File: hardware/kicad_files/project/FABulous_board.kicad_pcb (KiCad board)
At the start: 4 copper layers, 101.2 x 63.5 mm, 79 parts, among them J1 Conn_01x03_Pin, J10 Conn_01x03_Pin, J11 Conn_01x03_Pin, J12 Conn_01x05_Pin, J2 Conn_01x03_Pin, J3 Conn_01x03_Pin, J4 Conn_01x03_Pin, J5 Conn_01x02_Socket, J6 Conn_02x04_Odd_Even, J7 Conn_02x12_Odd_Even, J8 Conn_01x03_Pin, J9 Conn_01x03_Pin, SW1 Tactile Switch, T1 LOGO, U1 W25Q32FVSS, U10 SN74LVC1G125DCKR, U11 SI5351A-B-GTR, U4 GT-USB-7010ASV, U5 FT232H, U6 AMS1117-3_3, U7 SPX1117M3-L-1-5_TR, U8 MCP1319MT-29LE-OT, U9 SN74LVC1G125DCKR, X1 TXM12M0004252DBCEO00T, X2 NX3225GA-25_000M-STD-CRG-2

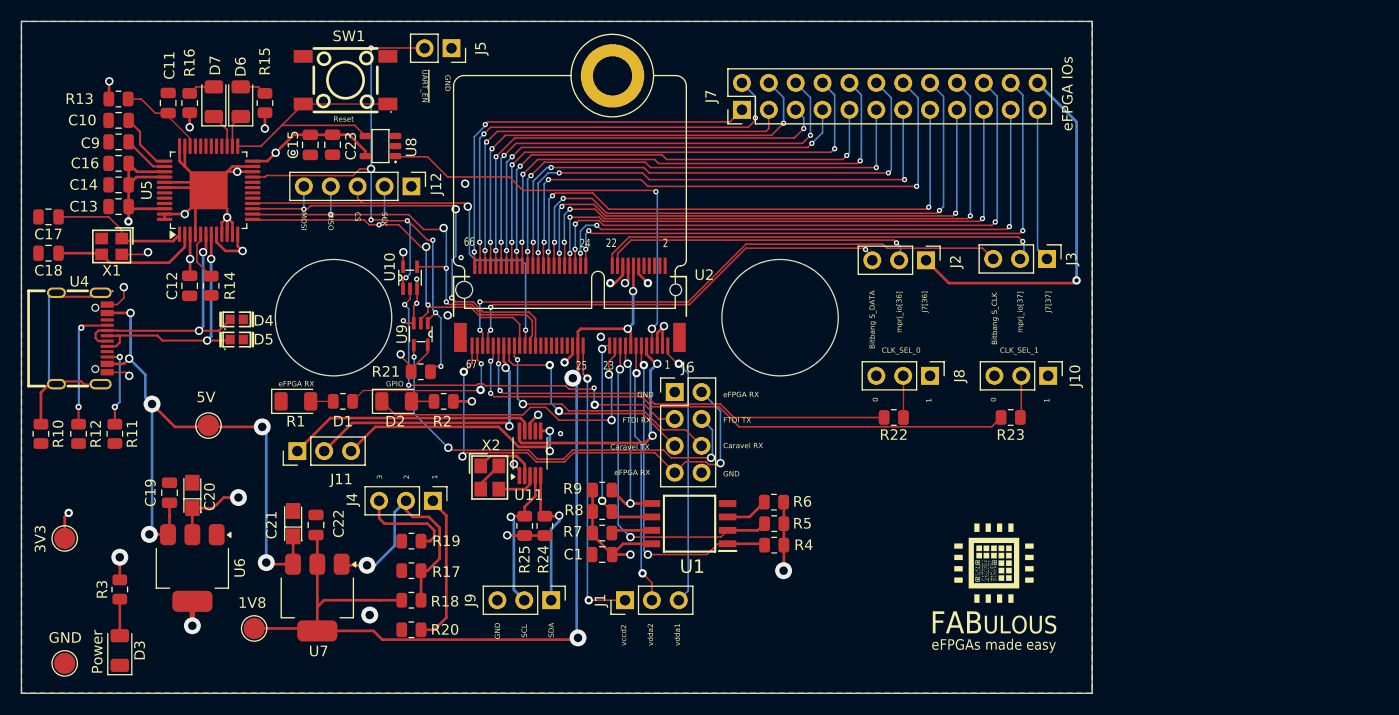
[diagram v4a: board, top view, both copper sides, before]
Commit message: feat: Implement all findings of the second review
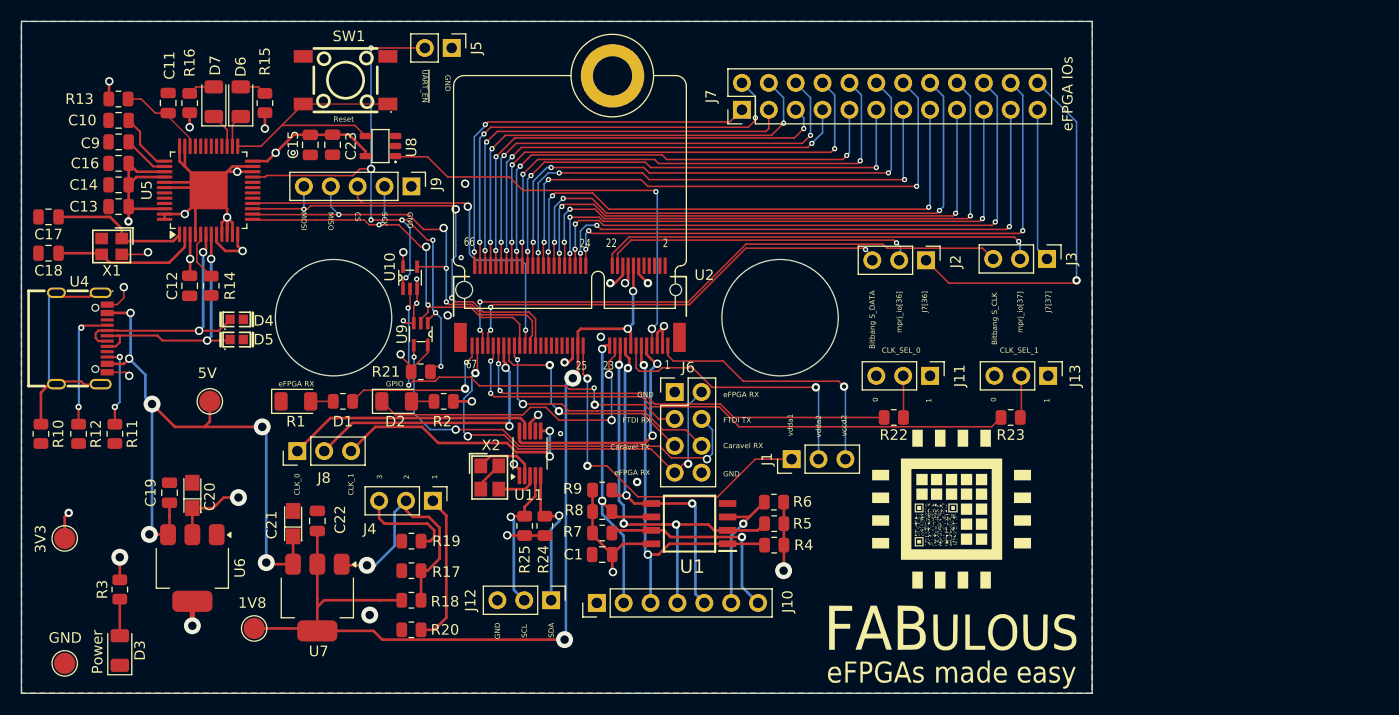
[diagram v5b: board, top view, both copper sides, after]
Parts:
- added J10: Conn_01x07_Pin, Connector_PinHeader_2.54mm:PinHeader_1x07_P2.54mm_Vertical, F.Cu at (158.0, 122.9)
- D1: value blue -> C434440
- D2: value red -> C3646938
- D3, D6, D7: value yellow green -> C965826
- J5: value Conn_01x02_Socket -> Conn_01x02_Pin; footprint Connector_PinSocket_2.54mm:PinSocket_1x02_P2.54mm_Vertical -> Connector_PinHeader_2.54mm:PinHeader_1x02_P2.54mm_Vertical
- T1: footprint FABulous:fabulous_logo_qr_code_generated -> FABulous:fabulous_logo_qr_code_generated_30mm
- U1: value W25Q32FVSS -> W25Q32JVSSIQ
- U2: value ~ -> C2977809
- moved J1 20.6 mm to (176.4, 109.3)
- moved T1 4.97 mm to (191.5, 118.4)
- moved TP2 2.29 mm to (121.4, 103.9)
- moved C22 0.40 mm to (131.6, 115.2)
- renumbered J8 to J11, J9 to J12, J10 to J13, J11 to J8, J12 to J9
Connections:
- net /Caravel_SPI.CS renamed /Flash_SPI.CS
- net /Caravel_SPI.DI renamed /Flash_SPI.POCI
- net /Caravel_SPI.DO renamed /Flash_SPI.PICO
- net /Caravel_SPI.SCK renamed /Flash_SPI.SCK
- net /FTDI_SPI.DI renamed /FTDI_SPI.POCI
- net /FTDI_SPI.DO renamed /FTDI_SPI.PICO
- net Net-(U1-~{HOLD}(D3)) renamed /~{Flash_HOLD}
- net Net-(U1-~{WP}(D2)) renamed /~{Flash_WP}
- U2 pad 73: /Caravel Connections/fpga_rx_led -> /efpga_uart_rx
- U2 pad 75: /efpga_uart_rx -> /Caravel Connections/fpga_rx_led
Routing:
- net /~{Flash_HOLD}: track 3.85 -> 19.5 mm, vias 0 -> 1
- net /Flash_SPI.PICO: track 19.4 -> 32.5 mm, vias 2 -> 3
- net /Flash_SPI.SCK: track 20.5 -> 31.0 mm
- net /~{Flash_WP}: track 4.04 -> 12.9 mm, vias 0 -> 1
- net /Flash_SPI.POCI: track 31.9 -> 38.4 mm, vias 2 -> 3
- net /Caravel Connections/vdda1: track 27.7 -> 33.5 mm
- net /efpga_uart_rx: track 44.9 -> 39.7 mm
- net /Flash_SPI.CS: track 31.5 -> 36.2 mm
- net +5V: track 61.0 -> 63.7 mm
- net /Caravel Connections/vdda2: track 24.8 -> 27.0 mm, vias 2 -> 1
- net /Caravel Connections/fpga_rx_led: track 16.9 -> 15.7 mm
- net +1V8: track 91.0 -> 89.9 mm
- net /FTDI_UART_TX: track 41.1 -> 40.4 mm
- net /CLK_efpga_1: track 23.4 -> 24.2 mm
- net /Caravel Connections/mprj_io_36_internal: track 42.6 -> 42.1 mm
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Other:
- board text added: "CLK_0"
- board text added: "CLK_1"

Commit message: feat: apply changes not saved before previous commit
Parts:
- moved J10 0.25 mm to (158.0, 122.7)
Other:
- board text added: "PICO"
- board text added: "POCI"
- board text added: "~{HOLD}"
- board text added: "~{WP}"
- board text removed: "MISO"
- board text removed: "MOSI"
